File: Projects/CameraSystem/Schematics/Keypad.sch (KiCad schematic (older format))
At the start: 26 parts, among them J11 Conn_01x06, J12 Conn_01x06, K1 TouchPad, K2 TouchPad, K3 TouchPad, K4 TouchPad, K5 TouchPad, K6 TouchPad, K7 TouchPad, Q3 BC846B_215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

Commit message: feat: symbol assignment updated
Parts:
- C26: footprint Capacitor_SMD:C_0603_1608Metric_Pad1.05x0.95mm_HandSolder -> digikey-footprints:0603
- K1, K2, K3, K4, K5, K6, K7: footprint (none) -> custom-footprints:QPad_Round_D10
- R31, R32, R33, R34, R35, R36, R37, R38, R39, R40, R41, R42, R43: footprint Resistor_SMD:R_0603_1608Metric_Pad1.05x0.95mm_HandSolder -> digikey-footprints:0603
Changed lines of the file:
@@
 F 0 "K3" H 7800 2550 60  0000 C CNN
 F 1 "TouchPad" H 7800 2950 60  0000 C CNN
-F 2 "" H 7850 2750 60  0001 C CNN
+F 2 "custom-footprints:QPad_Round_D10" H 7850 2750 60  0001 C CNN
 F 3 "" H 7850 2750 60  0001 C CNN
 	1    7800 2750
@@
 F 0 "R38" V 6130 3300 50  0000 C CNN
 F 1 "4K7" V 6050 3300 50  0000 C CNN
-F 2 "Resistor_SMD:R_0603_1608Metric_Pad1.05x0.95mm_HandSolder" V 5980 3300 50  0001 C CNN
+F 2 "digikey-footprints:0603" V 5980 3300 50  0001 C CNN
 F 3 "" H 6050 3300 50  0001 C CNN
 	1    6050 3300
@@
 F 0 "R41" V 6480 3400 50  0000 C CNN
 F 1 "4K7" V 6400 3400 50  0000 C CNN
-F 2 "Resistor_SMD:R_0603_1608Metric_Pad1.05x0.95mm_HandSolder" V 6330 3400 50  0001 C CNN
+F 2 "digikey-footprints:0603" V 6330 3400 50  0001 C CNN
 F 3 "" H 6400 3400 50  0001 C CNN
 	1    6400 3400
@@
 F 0 "R39" V 6130 3500 50  0000 C CNN
 F 1 "4K7" V 6050 3500 50  0000 C CNN
-F 2 "Resistor_SMD:R_0603_1608Metric_Pad1.05x0.95mm_HandSolder" V 5980 3500 50  0001 C CNN
+F 2 "digikey-footprints:0603" V 5980 3500 50  0001 C CNN
 F 3 "" H 6050 3500 50  0001 C CNN
 	1    6050 3500
@@
 F 0 "R42" V 6480 3600 50  0000 C CNN
 F 1 "4K7" V 6400 3600 50  0000 C CNN
-F 2 "Resistor_SMD:R_0603_1608Metric_Pad1.05x0.95mm_HandSolder" V 6330 3600 50  0001 C CNN
+F 2 "digikey-footprints:0603" V 6330 3600 50  0001 C CNN
 F 3 "" H 6400 3600 50  0001 C CNN
 	1    6400 3600
@@
 F 0 "R40" V 6130 3700 50  0000 C CNN
 F 1 "4K7" V 6050 3700 50  0000 C CNN
-F 2 "Resistor_SMD:R_0603_1608Metric_Pad1.05x0.95mm_HandSolder" V 5980 3700 50  0001 C CNN
+F 2 "digikey-footprints:0603" V 5980 3700 50  0001 C CNN
 F 3 "" H 6050 3700 50  0001 C CNN
 	1    6050 3700
@@
 F 0 "R43" V 6480 3800 50  0000 C CNN
 F 1 "4K7" V 6400 3800 50  0000 C CNN
-F 2 "Resistor_SMD:R_0603_1608Metric_Pad1.05x0.95mm_HandSolder" V 6330 3800 50  0001 C CNN
+F 2 "digikey-footprints:0603" V 6330 3800 50  0001 C CNN
 F 3 "" H 6400 3800 50  0001 C CNN
 	1    6400 3800
@@
 F 0 "R34" V 3930 3800 50  0000 C CNN
 F 1 "4K7" V 3850 3800 50  0000 C CNN
-F 2 "Resistor_SMD:R_0603_1608Metric_Pad1.05x0.95mm_HandSolder" V 3780 3800 50  0001 C CNN
+F 2 "digikey-footprints:0603" V 3780 3800 50  0001 C CNN
 F 3 "" H 3850 3800 50  0001 C CNN
 	1    3850 3800
@@
 F 0 "K5" H 7800 3650 60  0000 C CNN
 F 1 "TouchPad" H 7800 4050 60  0000 C CNN
-F 2 "" H 7850 3850 60  0001 C CNN
+F 2 "custom-footprints:QPad_Round_D10" H 7850 3850 60  0001 C CNN
 F 3 "" H 7850 3850 60  0001 C CNN
 	1    7800 3850
@@
 F 0 "K4" H 7800 3100 60  0000 C CNN
 F 1 "TouchPad" H 7800 3500 60  0000 C CNN
-F 2 "" H 7850 3300 60  0001 C CNN
+F 2 "custom-footprints:QPad_Round_D10" H 7850 3300 60  0001 C CNN
 F 3 "" H 7850 3300 60  0001 C CNN
 	1    7800 3300
@@
 F 0 "K2" H 7800 2050 60  0000 C CNN
 F 1 "TouchPad" H 7800 2450 60  0000 C CNN
-F 2 "" H 7850 2250 60  0001 C CNN
+F 2 "custom-footprints:QPad_Round_D10" H 7850 2250 60  0001 C CNN
 F 3 "" H 7850 2250 60  0001 C CNN
 	1    7800 2250
@@
 F 0 "K6" H 7800 4200 60  0000 C CNN
 F 1 "TouchPad" H 7800 4600 60  0000 C CNN
-F 2 "" H 7850 4400 60  0001 C CNN
+F 2 "custom-footprints:QPad_Round_D10" H 7850 4400 60  0001 C CNN
 F 3 "" H 7850 4400 60  0001 C CNN
 	1    7800 4400
@@
 F 0 "K7" H 7800 4750 60  0000 C CNN
 F 1 "TouchPad" H 7800 5150 60  0000 C CNN
-F 2 "" H 7850 4950 60  0001 C CNN
+F 2 "custom-footprints:QPad_Round_D10" H 7850 4950 60  0001 C CNN
 F 3 "" H 7850 4950 60  0001 C CNN
 	1    7800 4950
@@
 F 0 "K1" H 2800 3600 60  0000 C CNN
 F 1 "TouchPad" H 2800 4000 60  0000 C CNN
-F 2 "" H 2850 3800 60  0001 C CNN
+F 2 "custom-footprints:QPad_Round_D10" H 2850 3800 60  0001 C CNN
 F 3 "" H 2850 3800 60  0001 C CNN
 	1    2800 3800
@@
 F 0 "C26" H 4225 2800 50  0000 L CNN
 F 1 "100n" H 4225 2600 50  0000 L CNN
-F 2 "Capacitor_SMD:C_0603_1608Metric_Pad1.05x0.95mm_HandSolder" H 4238 2550 50  0001 C CNN
+F 2 "digikey-footprints:0603" H 4238 2550 50  0001 C CNN
 F 3 "" H 4200 2700 50  0001 C CNN
 	1    4200 2700
@@
 F 0 "R33" V 2630 5400 50  0000 C CNN
 F 1 "10K" V 2550 5400 50  0000 C CNN
-F 2 "Resistor_SMD:R_0603_1608Metric_Pad1.05x0.95mm_HandSolder" V 2480 5400 50  0001 C CNN
+F 2 "digikey-footprints:0603" V 2480 5400 50  0001 C CNN
 F 3 "" H 2550 5400 50  0001 C CNN
 	1    2550 5400
@@
 F 0 "R32" V 2130 6450 50  0000 C CNN
 F 1 "10K" V 2050 6450 50  0000 C CNN
-F 2 "Resistor_SMD:R_0603_1608Metric_Pad1.05x0.95mm_HandSolder" V 1980 6450 50  0001 C CNN
+F 2 "digikey-footprints:0603" V 1980 6450 50  0001 C CNN
 F 3 "" H 2050 6450 50  0001 C CNN
 	1    2050 6450
@@
 F 0 "R31" V 1780 6100 50  0000 C CNN
 F 1 "4K7" V 1700 6100 50  0000 C CNN
-F 2 "Resistor_SMD:R_0603_1608Metric_Pad1.05x0.95mm_HandSolder" V 1630 6100 50  0001 C CNN
+F 2 "digikey-footprints:0603" V 1630 6100 50  0001 C CNN
 F 3 "" H 1700 6100 50  0001 C CNN
 	1    1700 6100
@@
 F 0 "R37" V 5430 5400 50  0000 C CNN
 F 1 "10K" V 5350 5400 50  0000 C CNN
-F 2 "Resistor_SMD:R_0603_1608Metric_Pad1.05x0.95mm_HandSolder" V 5280 5400 50  0001 C CNN
+F 2 "digikey-footprints:0603" V 5280 5400 50  0001 C CNN
 F 3 "" H 5350 5400 50  0001 C CNN
 	1    5350 5400
@@
 F 0 "R36" V 4930 6450 50  0000 C CNN
 F 1 "10K" V 4850 6450 50  0000 C CNN
-F 2 "Resistor_SMD:R_0603_1608Metric_Pad1.05x0.95mm_HandSolder" V 4780 6450 50  0001 C CNN
+F 2 "digikey-footprints:0603" V 4780 6450 50  0001 C CNN
 F 3 "" H 4850 6450 50  0001 C CNN
 	1    4850 6450
@@
 F 0 "R35" V 4580 6100 50  0000 C CNN
 F 1 "4K7" V 4500 6100 50  0000 C CNN
-F 2 "Resistor_SMD:R_0603_1608Metric_Pad1.05x0.95mm_HandSolder" V 4430 6100 50  0001 C CNN
+F 2 "digikey-footprints:0603" V 4430 6100 50  0001 C CNN
 F 3 "" H 4500 6100 50  0001 C CNN
 	1    4500 6100

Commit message: feat: assign footprints
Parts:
- J11, J12: footprint (none) -> Pin_Headers:Pin_Header_Straight_1x06_Pitch2.54mm
- U10: footprint (none) -> custom-footprints:AT42QT1070-SSUR
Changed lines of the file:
@@
 F 0 "U10" H 5100 3000 60  0000 C CNN
 F 1 "AT42QT1070-SSUR" H 5100 4000 60  0000 C CNN
-F 2 "" H 5100 3500 60  0001 C CNN
+F 2 "custom-footprints:AT42QT1070-SSUR" H 5100 3500 60  0001 C CNN
 F 3 "" H 5100 3500 60  0001 C CNN
 	1    5100 3500
@@
 F 0 "J11" H 1830 3492 50  0000 L CNN
 F 1 "Conn_01x06" H 1830 3401 50  0000 L CNN
-F 2 "" H 1750 3500 50  0001 C CNN
+F 2 "Pin_Headers:Pin_Header_Straight_1x06_Pitch2.54mm" H 1750 3500 50  0001 C CNN
 F 3 "~" H 1750 3500 50  0001 C CNN
 	1    1750 3500
@@
 F 0 "J12" H 1830 4442 50  0000 L CNN
 F 1 "Conn_01x06" H 1830 4351 50  0000 L CNN
-F 2 "" H 1750 4450 50  0001 C CNN
+F 2 "Pin_Headers:Pin_Header_Straight_1x06_Pitch2.54mm" H 1750 4450 50  0001 C CNN
 F 3 "~" H 1750 4450 50  0001 C CNN
 	1    1750 4450

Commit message: feat: position components in layout
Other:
- moved on the sheet: J11, J12
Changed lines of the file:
@@
 $Descr A4 11693 8268
 encoding utf-8
-Sheet 8 9
+Sheet 7 9
 Title ""
 Date ""
@@
 L Connector_Generic:Conn_01x06 J11
 U 1 1 5BBF5B08
-P 1750 3500
-F 0 "J11" H 1830 3492 50  0000 L CNN
-F 1 "Conn_01x06" H 1830 3401 50  0000 L CNN
-F 2 "Pin_Headers:Pin_Header_Straight_1x06_Pitch2.54mm" H 1750 3500 50  0001 C CNN
-F 3 "~" H 1750 3500 50  0001 C CNN
-	1    1750 3500
+P 1750 3600
+F 0 "J11" H 1830 3592 50  0000 L CNN
+F 1 "Conn_01x06" H 1830 3501 50  0000 L CNN
+F 2 "Pin_Headers:Pin_Header_Straight_1x06_Pitch2.54mm" H 1750 3600 50  0001 C CNN
+F 3 "~" H 1750 3600 50  0001 C CNN
+	1    1750 3600
 	1    0    0    -1
 $EndComp
@@
 Text HLabel 1450 3400 0    60   BiDi ~ 0
 SDA_3V3_CON
-Text HLabel 1450 3300 0    60   Input ~ 0
+Text HLabel 1450 3900 0    60   Input ~ 0
 VDD_3V3_CON
 Wire Wire Line
-	1450 3300 1550 3300
+	1450 3900 1550 3900
 Wire Wire Line
 	1450 3400 1550 3400
@@
 L Connector_Generic:Conn_01x06 J12
 U 1 1 5BC19F1B
-P 1750 4450
-F 0 "J12" H 1830 4442 50  0000 L CNN
-F 1 "Conn_01x06" H 1830 4351 50  0000 L CNN
-F 2 "Pin_Headers:Pin_Header_Straight_1x06_Pitch2.54mm" H 1750 4450 50  0001 C CNN
-F 3 "~" H 1750 4450 50  0001 C CNN
-	1    1750 4450
-	1    0    0    -1
-$EndComp
-Wire Wire Line
-	1450 4250 1550 4250
+P 1750 4550
+F 0 "J12" H 1830 4542 50  0000 L CNN
+F 1 "Conn_01x06" H 1830 4451 50  0000 L CNN
+F 2 "Pin_Headers:Pin_Header_Straight_1x06_Pitch2.54mm" H 1750 4550 50  0001 C CNN
+F 3 "~" H 1750 4550 50  0001 C CNN
+	1    1750 4550
+	1    0    0    -1
+$EndComp
+Wire Wire Line
+	1450 4850 1550 4850
 Wire Wire Line
 	1450 4350 1550 4350
@@
 Wire Wire Line
 	1450 4750 1550 4750
-Text Label 1450 4250 2    60   ~ 0
+Text Label 1450 4850 2    60   ~ 0
 VDD_3V3
 Text Label 1450 4350 2    60   ~ 0

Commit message: feat: update layout
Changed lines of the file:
@@
 Text HLabel 1450 3700 0    60   Input ~ 0
 QT_CHN_CON
-Text HLabel 1450 3600 0    60   Input ~ 0
+Text HLabel 1450 3400 0    60   Input ~ 0
 SCL_3V3_CON
-Text HLabel 1450 3400 0    60   BiDi ~ 0
+Text HLabel 1450 3600 0    60   BiDi ~ 0
 SDA_3V3_CON
 Text HLabel 1450 3900 0    60   Input ~ 0
@@
 Text Label 1450 4850 2    60   ~ 0
 VDD_3V3
-Text Label 1450 4350 2    60   ~ 0
+Text Label 1450 4550 2    60   ~ 0
 SDA_3V3
 Text Label 1450 4450 2    60   ~ 0
 QP_GND
-Text Label 1450 4550 2    60   ~ 0
+Text Label 1450 4350 2    60   ~ 0
 SCL_3V3
 Text Label 1450 4650 2    60   ~ 0

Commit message: Camera System QT Pad schematic reviewed
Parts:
- removed Q4: BC846B_215, digikey-footprints:SOT-23-3, symbol CameraSystem-rescue:BC846B_215
- removed R35: 4K7, digikey-footprints:0603, symbol Device:R
- removed R36: 10K, digikey-footprints:0603, symbol Device:R
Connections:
- net labels removed: _QT_CHN_IN
- wire segments 84 -> 74
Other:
- moved on the sheet: R37
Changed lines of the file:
@@
 U 1 1 5BBEAF3D
 P 2800 3800
-F 0 "K1" H 2800 3600 60  0000 C CNN
+F 0 "K1" H 2850 4150 60  0000 C CNN
 F 1 "TouchPad" H 2800 4000 60  0000 C CNN
 F 2 "custom-footprints:QPad_Round_D10" H 2850 3800 60  0001 C CNN
@@
 Wire Wire Line
 	4450 3500 3650 3500
-Wire Wire Line
-	4450 3600 3650 3600
 Text Label 3650 3500 0    60   ~ 0
 _QT_RST_IN
-Text Label 3650 3600 0    60   ~ 0
-_QT_CHN_IN
 $Comp
 L CameraSystem-rescue:BC846B_215 Q?
@@
 _QT_RST_IN
 $Comp
-L CameraSystem-rescue:BC846B_215 Q?
-U 1 1 5BBEE372
-P 5250 6100
-AR Path="/5BBEE372" Ref="Q?"  Part="1"
-AR Path="/5BBB389E/5BBEE372" Ref="Q4"  Part="1"
-F 0 "Q4" H 5124 6266 60  0000 L CNN
-F 1 "BC846B_215" V 5456 6100 60  0000 C CNN
-F 2 "digikey-footprints:SOT-23-3" H 5450 6300 60  0001 L CNN
-F 3 "https://assets.nexperia.com/documents/data-sheet/BC846_SER.pdf" H 5450 6400 60  0001 L CNN
-F 4 "1727-2920-1-ND" H 5450 6500 60  0001 L CNN "Digi-Key_PN"
-F 5 "BC846B,215" H 5450 6600 60  0001 L CNN "MPN"
-F 6 "Discrete Semiconductor Products" H 5450 6700 60  0001 L CNN "Category"
-F 7 "Transistors - Bipolar (BJT) - Single" H 5450 6800 60  0001 L CNN "Family"
-F 8 "https://assets.nexperia.com/documents/data-sheet/BC846_SER.pdf" H 5450 6900 60  0001 L CNN "DK_Datasheet_Link"
-F 9 "/product-detail/en/nexperia-usa-inc/BC846B,215/1727-2920-1-ND/763459" H 5450 7000 60  0001 L CNN "DK_Detail_Page"
-F 10 "TRANS NPN 65V 0.1A SOT23" H 5450 7100 60  0001 L CNN "Description"
-F 11 "Nexperia USA Inc." H 5450 7200 60  0001 L CNN "Manufacturer"
-F 12 "Active" H 5450 7300 60  0001 L CNN "Status"
-	1    5250 6100
-	1    0    0    -1
-$EndComp
-$Comp
 L Device:R R37
 U 1 1 5BBEE378
-P 5350 5400
-F 0 "R37" V 5430 5400 50  0000 C CNN
-F 1 "10K" V 5350 5400 50  0000 C CNN
-F 2 "digikey-footprints:0603" V 5280 5400 50  0001 C CNN
-F 3 "" H 5350 5400 50  0001 C CNN
-	1    5350 5400
+P 3150 3100
+F 0 "R37" V 3230 3100 50  0000 C CNN
+F 1 "10K" V 3150 3100 50  0000 C CNN
+F 2 "digikey-footprints:0603" V 3080 3100 50  0001 C CNN
+F 3 "" H 3150 3100 50  0001 C CNN
+	1    3150 3100
 	-1   0    0    1
 $EndComp
 Wire Wire Line
-	5350 5900 5350 5700
-Wire Wire Line
-	4650 6100 4850 6100
-Wire Wire Line
-	4850 6100 4850 6300
-$Comp
-L Device:R R36
-U 1 1 5BBEE381
-P 4850 6450
-F 0 "R36" V 4930 6450 50  0000 C CNN
-F 1 "10K" V 4850 6450 50  0000 C CNN
-F 2 "digikey-footprints:0603" V 4780 6450 50  0001 C CNN
-F 3 "" H 4850 6450 50  0001 C CNN
-	1    4850 6450
-	-1   0    0    1
-$EndComp
-Wire Wire Line
-	4850 6600 4850 6750
-Wire Wire Line
-	5350 6300 5350 6750
-$Comp
-L Device:R R35
-U 1 1 5BBEE395
-P 4500 6100
-F 0 "R35" V 4580 6100 50  0000 C CNN
-F 1 "4K7" V 4500 6100 50  0000 C CNN
-F 2 "digikey-footprints:0603" V 4430 6100 50  0001 C CNN
-F 3 "" H 4500 6100 50  0001 C CNN
-	1    4500 6100
-	0    -1   -1   0
-$EndComp
-Connection ~ 4850 6100
-Wire Wire Line
-	4350 6100 4150 6100
-Wire Wire Line
-	5350 5250 5350 4950
-Wire Wire Line
-	5350 4950 5450 4950
-Text Label 5450 4950 0    60   ~ 0
+	3150 2950 3150 2650
+Wire Wire Line
+	3150 2650 3250 2650
+Text Label 3250 2650 0    60   ~ 0
 VDD_3V3
 Wire Wire Line
-	5350 5700 5950 5700
-Connection ~ 5350 5700
-Text Label 5950 5700 0    60   ~ 0
-_QT_CHN_IN
-Wire Wire Line
 	3950 3200 4450 3200
 Wire Wire Line
@@
 Wire Wire Line
 	2550 5700 2550 5550
-Wire Wire Line
-	4850 6100 5050 6100
-Wire Wire Line
-	5350 5700 5350 5550
 $Comp
 L Connector_Generic:Conn_01x06 J11
@@
 Text HLabel 1450 3800 0    60   Input ~ 0
 QT_RST_CON
-Text HLabel 1450 3700 0    60   Input ~ 0
+Text HLabel 1450 3700 0    60   Output ~ 0
 QT_CHN_CON
 Text HLabel 1450 3400 0    60   Input ~ 0
@@
 QP_GND
 Wire Wire Line
-	4850 6750 5350 6750
-Wire Wire Line
-	5350 6750 5350 6850
-Wire Wire Line
-	5350 6850 5450 6850
-Connection ~ 5350 6750
-Text Label 5450 6850 0    60   ~ 0
-QP_GND
-Wire Wire Line
 	4350 4200 4450 4200
 Wire Wire Line
@@
 Text Label 1350 6100 2    60   ~ 0
 QT_RST
-Text Label 4150 6100 2    60   ~ 0
-QT_CHN
 Text Label 3650 3200 2    60   ~ 0
 VDD_3V3
@@
 	1    0    0    -1
 $EndComp
+Wire Wire Line
+	3150 3250 3150 3600
+Connection ~ 3150 3600
+Wire Wire Line
+	3150 3600 4450 3600
+Wire Wire Line
+	2700 3600 3150 3600
+Text Label 2700 3600 0    60   ~ 0
+QT_CHN
 $EndSCHEMATC

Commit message: replace tvs diodes of camera system
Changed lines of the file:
@@
 L cl-misc:TouchPad K3
 U 1 1 5BBEA57E
-P 7800 2750
-F 0 "K3" H 7800 2550 60  0000 C CNN
-F 1 "TouchPad" H 7800 2950 60  0000 C CNN
-F 2 "custom-footprints:QPad_Round_D10" H 7850 2750 60  0001 C CNN
-F 3 "" H 7850 2750 60  0001 C CNN
-	1    7800 2750
+P 7650 2750
+F 0 "K3" H 7650 2550 60  0000 C CNN
+F 1 "TouchPad" H 7650 2950 60  0000 C CNN
+F 2 "custom-footprints:QPad_Round_D10" H 7700 2750 60  0001 C CNN
+F 3 "" H 7700 2750 60  0001 C CNN
+	1    7650 2750
 	1    0    0    -1
 $EndComp
@@
 L cl-misc:TouchPad K5
 U 1 1 5BBEAA5F
-P 7800 3850
-F 0 "K5" H 7800 3650 60  0000 C CNN
-F 1 "TouchPad" H 7800 4050 60  0000 C CNN
-F 2 "custom-footprints:QPad_Round_D10" H 7850 3850 60  0001 C CNN
-F 3 "" H 7850 3850 60  0001 C CNN
-	1    7800 3850
+P 7650 3850
+F 0 "K5" H 7650 3650 60  0000 C CNN
+F 1 "TouchPad" H 7650 4050 60  0000 C CNN
+F 2 "custom-footprints:QPad_Round_D10" H 7700 3850 60  0001 C CNN
+F 3 "" H 7700 3850 60  0001 C CNN
+	1    7650 3850
 	1    0    0    -1
 $EndComp
@@
 L cl-misc:TouchPad K4
 U 1 1 5BBEAAB3
-P 7800 3300
-F 0 "K4" H 7800 3100 60  0000 C CNN
-F 1 "TouchPad" H 7800 3500 60  0000 C CNN
-F 2 "custom-footprints:QPad_Round_D10" H 7850 3300 60  0001 C CNN
-F 3 "" H 7850 3300 60  0001 C CNN
-	1    7800 3300
+P 7650 3300
+F 0 "K4" H 7650 3100 60  0000 C CNN
+F 1 "TouchPad" H 7650 3500 60  0000 C CNN
+F 2 "custom-footprints:QPad_Round_D10" H 7700 3300 60  0001 C CNN
+F 3 "" H 7700 3300 60  0001 C CNN
+	1    7650 3300
 	1    0    0    -1
 $EndComp
@@
 L cl-misc:TouchPad K2
 U 1 1 5BBEAAF6
-P 7800 2250
-F 0 "K2" H 7800 2050 60  0000 C CNN
-F 1 "TouchPad" H 7800 2450 60  0000 C CNN
-F 2 "custom-footprints:QPad_Round_D10" H 7850 2250 60  0001 C CNN
-F 3 "" H 7850 2250 60  0001 C CNN
-	1    7800 2250
+P 7650 2250
+F 0 "K2" H 7650 2050 60  0000 C CNN
+F 1 "TouchPad" H 7650 2450 60  0000 C CNN
+F 2 "custom-footprints:QPad_Round_D10" H 7700 2250 60  0001 C CNN
+F 3 "" H 7700 2250 60  0001 C CNN
+	1    7650 2250
 	1    0    0    -1
 $EndComp
@@
 L cl-misc:TouchPad K6
 U 1 1 5BBEAD74
-P 7800 4400
-F 0 "K6" H 7800 4200 60  0000 C CNN
-F 1 "TouchPad" H 7800 4600 60  0000 C CNN
-F 2 "custom-footprints:QPad_Round_D10" H 7850 4400 60  0001 C CNN
-F 3 "" H 7850 4400 60  0001 C CNN
-	1    7800 4400
+P 7650 4400
+F 0 "K6" H 7650 4200 60  0000 C CNN
+F 1 "TouchPad" H 7650 4600 60  0000 C CNN
+F 2 "custom-footprints:QPad_Round_D10" H 7700 4400 60  0001 C CNN
+F 3 "" H 7700 4400 60  0001 C CNN
+	1    7650 4400
 	1    0    0    -1
 $EndComp
@@
 L cl-misc:TouchPad K7
 U 1 1 5BBEADBD
-P 7800 4950
-F 0 "K7" H 7800 4750 60  0000 C CNN
-F 1 "TouchPad" H 7800 5150 60  0000 C CNN
-F 2 "custom-footprints:QPad_Round_D10" H 7850 4950 60  0001 C CNN
-F 3 "" H 7850 4950 60  0001 C CNN
-	1    7800 4950
+P 7650 4950
+F 0 "K7" H 7650 4750 60  0000 C CNN
+F 1 "TouchPad" H 7650 5150 60  0000 C CNN
+F 2 "custom-footprints:QPad_Round_D10" H 7700 4950 60  0001 C CNN
+F 3 "" H 7700 4950 60  0001 C CNN
+	1    7650 4950
 	1    0    0    -1
 $EndComp

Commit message: linux adaptation
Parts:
- K1, K2, K3, K4, K5, K6, K7: symbol cl-misc:TouchPad -> CameraSystem-rescue:TouchPad-cl-misc
- U10: symbol cl-integrated_circuits:AT42QT1070-SSUR -> CameraSystem-rescue:AT42QT1070-SSUR-cl-integrated_circuits
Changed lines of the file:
@@
 $EndDescr
 $Comp
-L cl-integrated_circuits:AT42QT1070-SSUR U10
+L CameraSystem-rescue:AT42QT1070-SSUR-cl-integrated_circuits U10
 U 1 1 5BBEA4BE
 P 5100 3500
+AR Path="/5BBEA4BE" Ref="U10"  Part="1"
+AR Path="/5BBB389E/5BBEA4BE" Ref="U10"  Part="1"
 F 0 "U10" H 5100 3000 60  0000 C CNN
 F 1 "AT42QT1070-SSUR" H 5100 4000 60  0000 C CNN
@@
 $EndComp
 $Comp
-L cl-misc:TouchPad K3
+L CameraSystem-rescue:TouchPad-cl-misc K3
 U 1 1 5BBEA57E
 P 7650 2750
+AR Path="/5BBEA57E" Ref="K3"  Part="1"
+AR Path="/5BBB389E/5BBEA57E" Ref="K3"  Part="1"
 F 0 "K3" H 7650 2550 60  0000 C CNN
 F 1 "TouchPad" H 7650 2950 60  0000 C CNN
@@
 	5750 3800 6250 3800
 $Comp
-L cl-misc:TouchPad K5
+L CameraSystem-rescue:TouchPad-cl-misc K5
 U 1 1 5BBEAA5F
 P 7650 3850
+AR Path="/5BBEAA5F" Ref="K5"  Part="1"
+AR Path="/5BBB389E/5BBEAA5F" Ref="K5"  Part="1"
 F 0 "K5" H 7650 3650 60  0000 C CNN
 F 1 "TouchPad" H 7650 4050 60  0000 C CNN
@@
 $EndComp
 $Comp
-L cl-misc:TouchPad K4
+L CameraSystem-rescue:TouchPad-cl-misc K4
 U 1 1 5BBEAAB3
 P 7650 3300
+AR Path="/5BBEAAB3" Ref="K4"  Part="1"
+AR Path="/5BBB389E/5BBEAAB3" Ref="K4"  Part="1"
 F 0 "K4" H 7650 3100 60  0000 C CNN
 F 1 "TouchPad" H 7650 3500 60  0000 C CNN
@@
 $EndComp
 $Comp
-L cl-misc:TouchPad K2
+L CameraSystem-rescue:TouchPad-cl-misc K2
 U 1 1 5BBEAAF6
 P 7650 2250
+AR Path="/5BBEAAF6" Ref="K2"  Part="1"
+AR Path="/5BBB389E/5BBEAAF6" Ref="K2"  Part="1"
 F 0 "K2" H 7650 2050 60  0000 C CNN
 F 1 "TouchPad" H 7650 2450 60  0000 C CNN
@@
 $EndComp
 $Comp
-L cl-misc:TouchPad K6
+L CameraSystem-rescue:TouchPad-cl-misc K6
 U 1 1 5BBEAD74
 P 7650 4400
+AR Path="/5BBEAD74" Ref="K6"  Part="1"
+AR Path="/5BBB389E/5BBEAD74" Ref="K6"  Part="1"
 F 0 "K6" H 7650 4200 60  0000 C CNN
 F 1 "TouchPad" H 7650 4600 60  0000 C CNN
@@
 $EndComp
 $Comp
-L cl-misc:TouchPad K7
+L CameraSystem-rescue:TouchPad-cl-misc K7
 U 1 1 5BBEADBD
 P 7650 4950
+AR Path="/5BBEADBD" Ref="K7"  Part="1"
+AR Path="/5BBB389E/5BBEADBD" Ref="K7"  Part="1"
 F 0 "K7" H 7650 4750 60  0000 C CNN
 F 1 "TouchPad" H 7650 5150 60  0000 C CNN
@@
 $EndComp
 $Comp
-L cl-misc:TouchPad K1
+L CameraSystem-rescue:TouchPad-cl-misc K1
 U 1 1 5BBEAF3D
 P 2800 3800
+AR Path="/5BBEAF3D" Ref="K1"  Part="1"
+AR Path="/5BBB389E/5BBEAF3D" Ref="K1"  Part="1"
 F 0 "K1" H 2850 4150 60  0000 C CNN
 F 1 "TouchPad" H 2800 4000 60  0000 C CNN

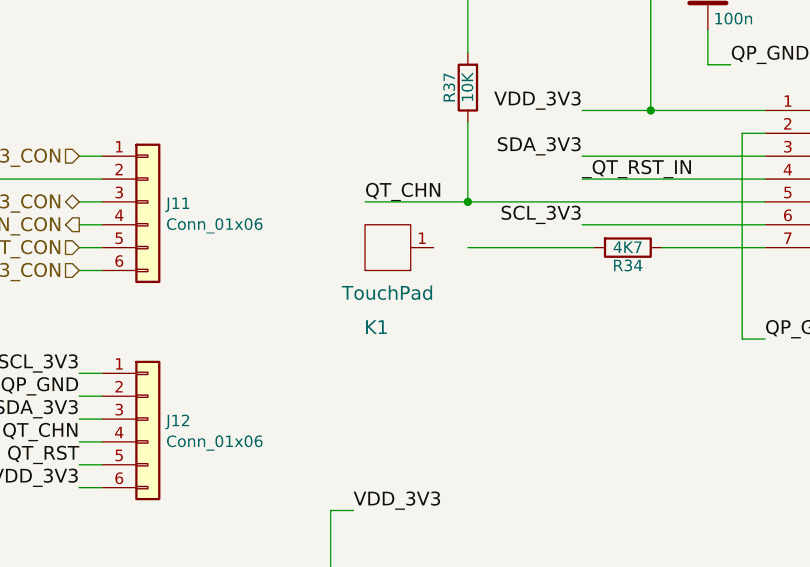
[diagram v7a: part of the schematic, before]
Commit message: wifi module added
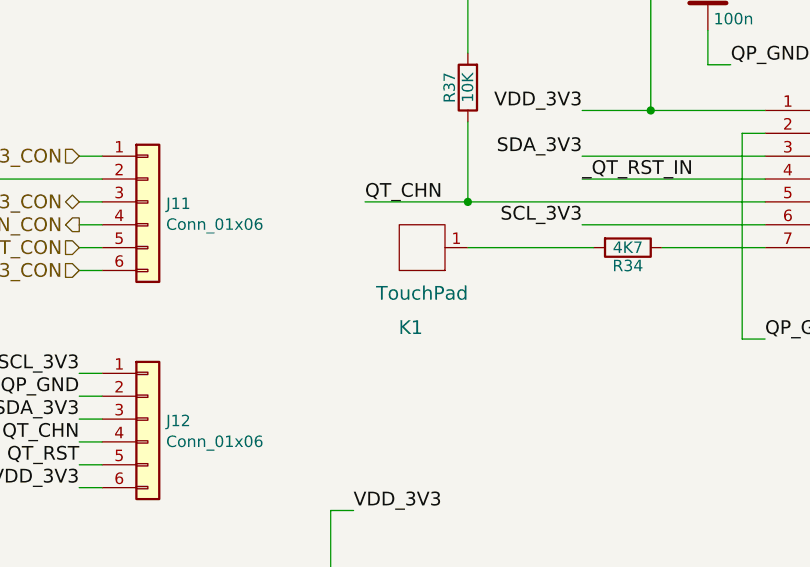
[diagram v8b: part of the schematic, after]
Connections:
- net at R34.2: now also K1.1
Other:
- moved on the sheet: K1
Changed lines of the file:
@@
 L CameraSystem-rescue:TouchPad-cl-misc K1
 U 1 1 5BBEAF3D
-P 2800 3800
+P 2950 3800
 AR Path="/5BBEAF3D" Ref="K1"  Part="1"
 AR Path="/5BBB389E/5BBEAF3D" Ref="K1"  Part="1"
-F 0 "K1" H 2850 4150 60  0000 C CNN
-F 1 "TouchPad" H 2800 4000 60  0000 C CNN
-F 2 "custom-footprints:QPad_Round_D10" H 2850 3800 60  0001 C CNN
-F 3 "" H 2850 3800 60  0001 C CNN
-	1    2800 3800
+F 0 "K1" H 3000 4150 60  0000 C CNN
+F 1 "TouchPad" H 2950 4000 60  0000 C CNN
+F 2 "custom-footprints:QPad_Round_D10" H 3000 3800 60  0001 C CNN
+F 3 "" H 3000 3800 60  0001 C CNN
+	1    2950 3800
 	-1   0    0    1
 $EndComp
